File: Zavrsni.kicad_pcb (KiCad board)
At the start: 2 copper layers, 70 x 133.3 mm, 42 parts, among them K1 JST-2pin-SMD, SW1 SW_Push, SW2 SW_Push, SW3 Power_switch

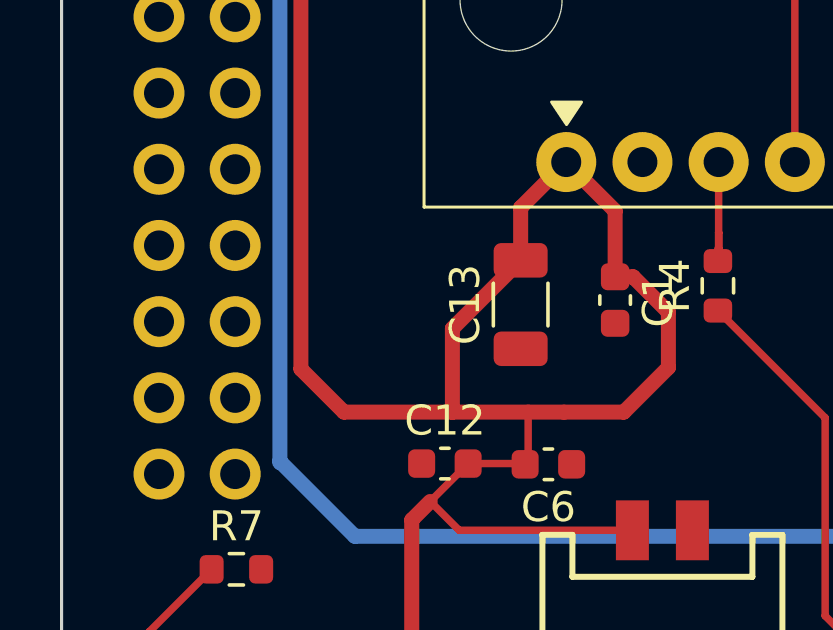
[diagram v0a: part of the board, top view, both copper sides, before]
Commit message: switch error, the wrong switch was selected and connected incorrectly in the schematic
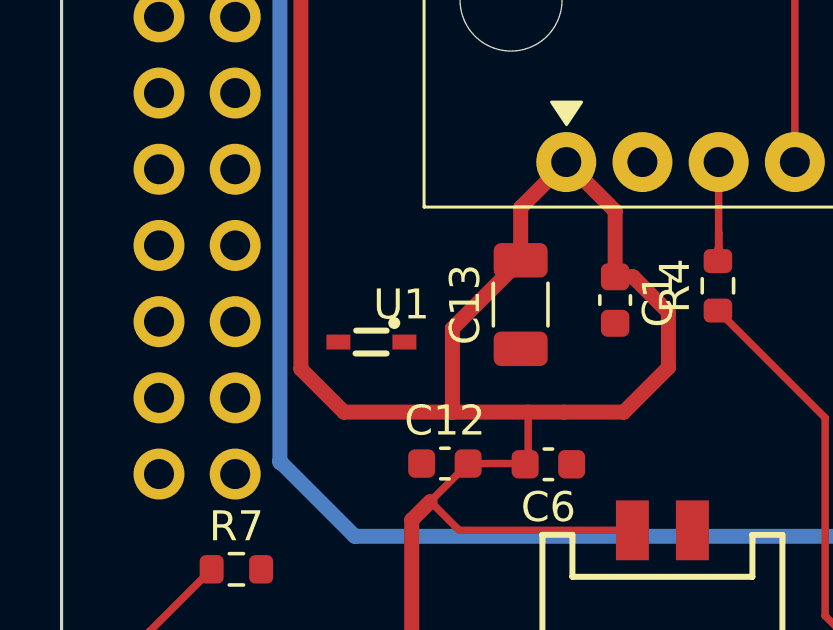
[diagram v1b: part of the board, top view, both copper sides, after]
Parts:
- added U1: Shottky_Diode, Schottky_Diode:Sh_D bat20, F.Cu at (75.2, 145.2)
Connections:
- NUCLEO_144_H743ZI2 pad 15: unconnected-(NUCLEO_144_H743ZI2-VIN-Pad15) -> /VIN

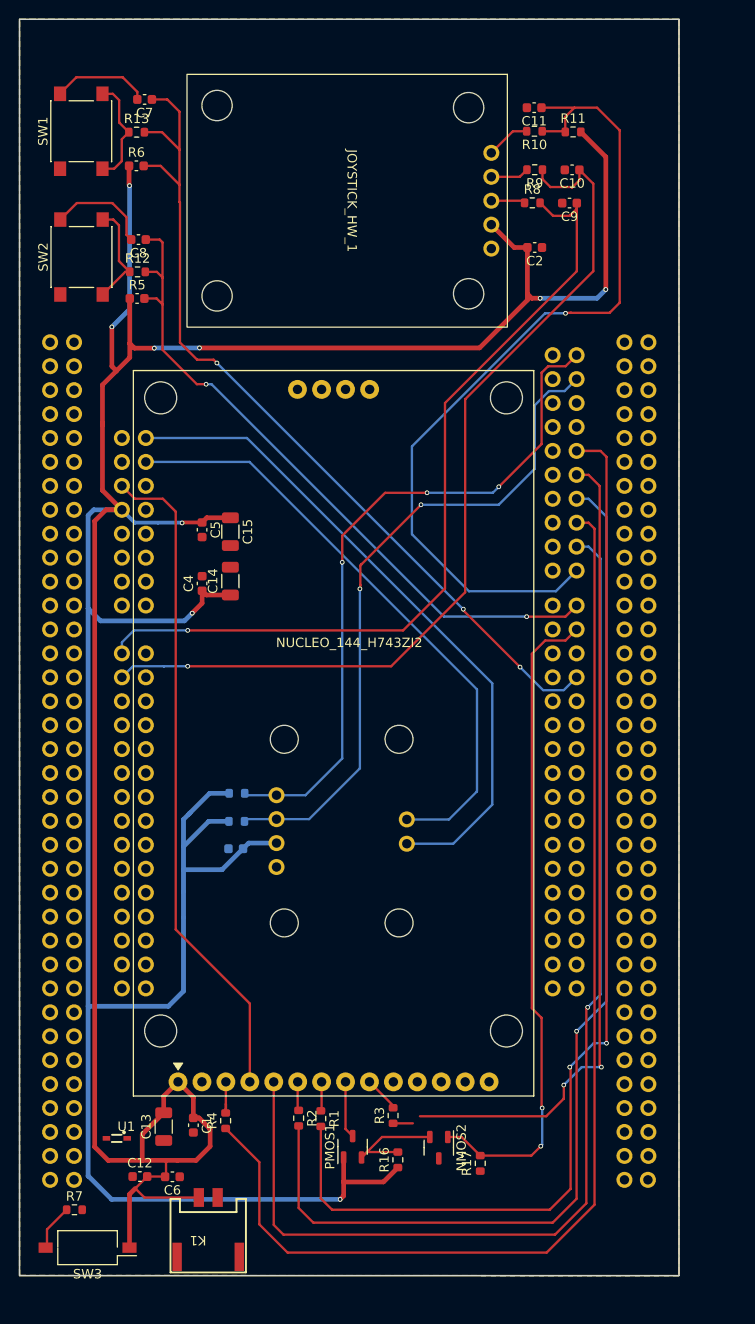
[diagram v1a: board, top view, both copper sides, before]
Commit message: Shifted pins on the nucleo board, up the y axis
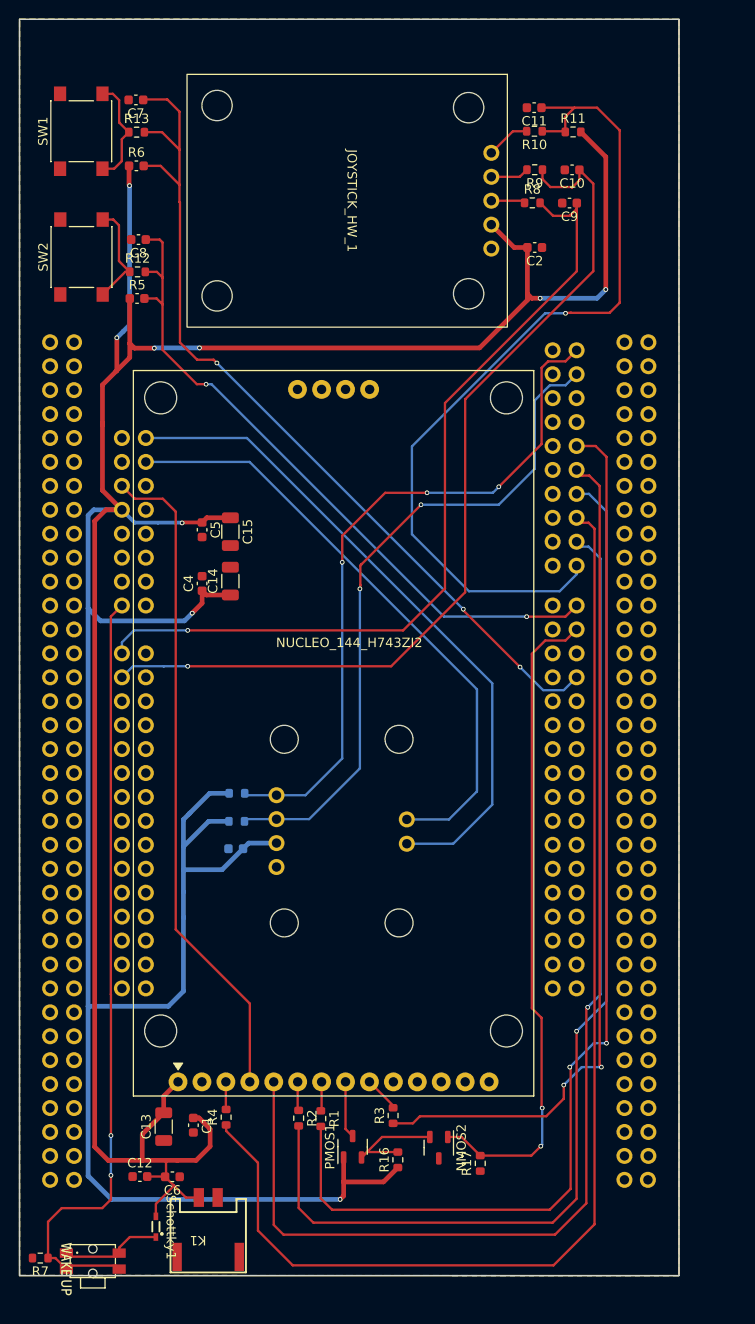
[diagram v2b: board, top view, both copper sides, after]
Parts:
- removed SW3: Power_switch, Button_Switch_SMD:SW_DIP_SPSTx01_Slide_Omron_A6S-110x_W8.9mm_P2.54mm
- removed U1: Shottky_Diode, Schottky_Diode:Sh_D bat20
- added Schottky1: ~, Schottky_D:Schottky_D, F.Cu at (79.5, 154.5)
- added Wake_up1: ~, Power_Switch:Power_Switch, F.Cu at (72.8, 158.8)
- moved R7 6.28 mm to (67.1, 157.8), turned to 180 degrees
- moved C7 0.93 mm to (77.3, 34.9)
- moved R4 0.38 mm to (86.8, 142.9)
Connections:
- NUCLEO_144_H743ZI2 pad 27: (no net) -> unconnected-(NUCLEO_144_H743ZI2-A5-Pad27)
- NUCLEO_144_H743ZI2 pad 30: (no net) -> unconnected-(NUCLEO_144_H743ZI2-PE2-Pad30)
- NUCLEO_144_H743ZI2 pad 94: (no net) -> unconnected-(NUCLEO_144_H743ZI2-PE_12(SCK/SPI4)-Pad94)
- R7 pad 1: Net-(R7-Pad1) -> /VIN
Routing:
- net /VIN: track 0.00 -> 83.4 mm, vias 0 -> 2
- net Earth: track 21.5 -> 0.22 mm
- net +3.3V: track 445.7 -> 433.9 mm
- net Net-(Schottky1-C): track 0.00 -> 10.8 mm
- net Net-(R7-Pad1): track 4.89 -> 0.00 mm
- net /CSN: track 124.5 -> 127.9 mm
- net /SDO(MISO): track 89.1 -> 90.4 mm
- net /D4: track 95.2 -> 96.2 mm
- net /CS: track 3.87 -> 2.94 mm
- net /SW: track 91.8 -> 92.5 mm
- net /SDI(MOSI): track 117.6 -> 118.1 mm
- net /D15: track 72.9 -> 73.5 mm
- net /D14: track 71.3 -> 71.8 mm

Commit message: The pcb is assembled, but the pin spacing is incorrect
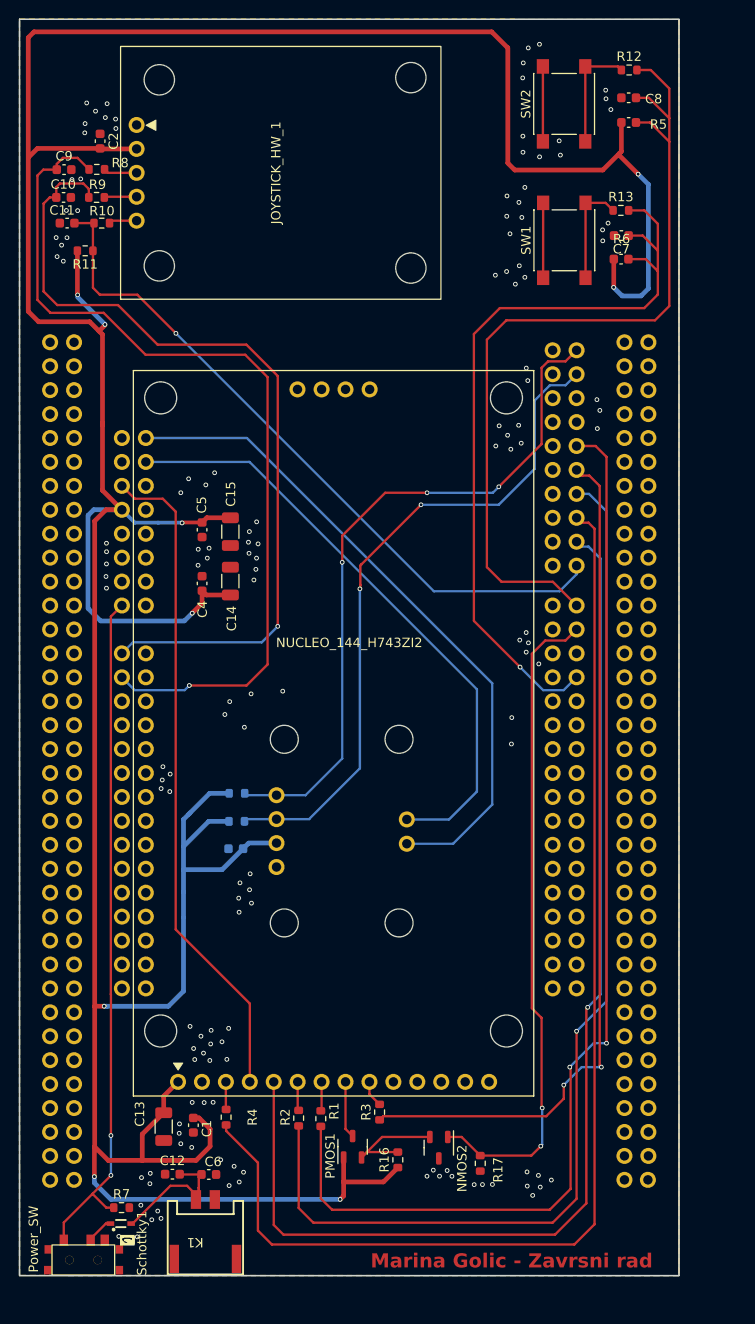
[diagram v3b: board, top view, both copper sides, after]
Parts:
- removed Wake_up1: ~, Power_Switch:Power_Switch
- added SW_Power1: ~, Power_Switch:Power_Switch, F.Cu at (72.0, 157.7)
- moved R12 56.4 mm to (129.6, 31.8)
- moved R5 55.4 mm to (129.6, 37.3)
- moved C8 54.2 mm to (129.6, 34.7)
- moved C10 54.1 mm to (69.6, 45.3), turned to 0 degrees
- moved C9 53.8 mm to (69.7, 42.3), turned to 0 degrees
- moved SW2 53.7 mm to (122.7, 35.4)
- moved C7 53.5 mm to (128.8, 49.3)
- moved R11 53.3 mm to (71.9, 50.9), turned to 180 degrees
- moved SW1 52.6 mm to (122.8, 49.8)
- moved R6 52.4 mm to (128.8, 51.8)
- moved R13 52.1 mm to (128.8, 46.6)
- moved C11 51.1 mm to (70.0, 48.0)
- moved C2 47.5 mm to (73.5, 39.3), turned to -90 degrees
- moved R10 46.9 mm to (73.7, 48.0), turned to 0 degrees
- moved R9 46.6 mm to (73.1, 45.3), turned to 0 degrees
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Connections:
- net /INT1 renamed /PC_8
- net /INT2 renamed /PC_9
- C12 pad 2: +3.3V -> /VBAT
- C6 pad 2: +3.3V -> /VBAT
- K1 pad 1: +3.3V -> /VBAT
- NUCLEO_144_H743ZI2 pad 17: /VRx -> /VRy
- NUCLEO_144_H743ZI2 pad 19: /VRy -> /VRx
- NUCLEO_144_H743ZI2 pad 28: unconnected-(NUCLEO_144_H743ZI2-GND-Pad28) -> Earth
- NUCLEO_144_H743ZI2 pad 71: unconnected-(NUCLEO_144_H743ZI2-GND-Pad71) -> Earth
- Schottky1 pad 1: +3.3V -> /VBAT
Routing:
- net /D7: track 73.8 -> 92.3 mm, vias 2 -> 0
- net /SW: track 92.5 -> 75.3 mm
- net +3.3V: track 433.9 -> 417.4 mm
- net /VBAT: track 0.00 -> 15.7 mm
- net Earth: track 0.22 -> 15.9 mm, vias 0 -> 144
- net /D4: track 96.2 -> 84.9 mm, vias 3 -> 1
- net /VIN: track 83.4 -> 72.8 mm
- net /VRy: track 98.0 -> 89.7 mm
- net Net-(Schottky1-C): track 10.8 -> 2.92 mm
- net /VRx: track 89.9 -> 95.8 mm
- net /CSN: track 127.9 -> 126.0 mm
- net /T1: track 4.70 -> 2.98 mm
- net /SDO(MISO): track 90.4 -> 91.7 mm
- net /SDO: track 3.79 -> 2.83 mm
- net Net-(R12-Pad1): track 11.3 -> 11.9 mm
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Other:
- board text added: "Marina Golic - Zavrsni rad"

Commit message: The pcb is cut for the buttons on the NUCLEO board
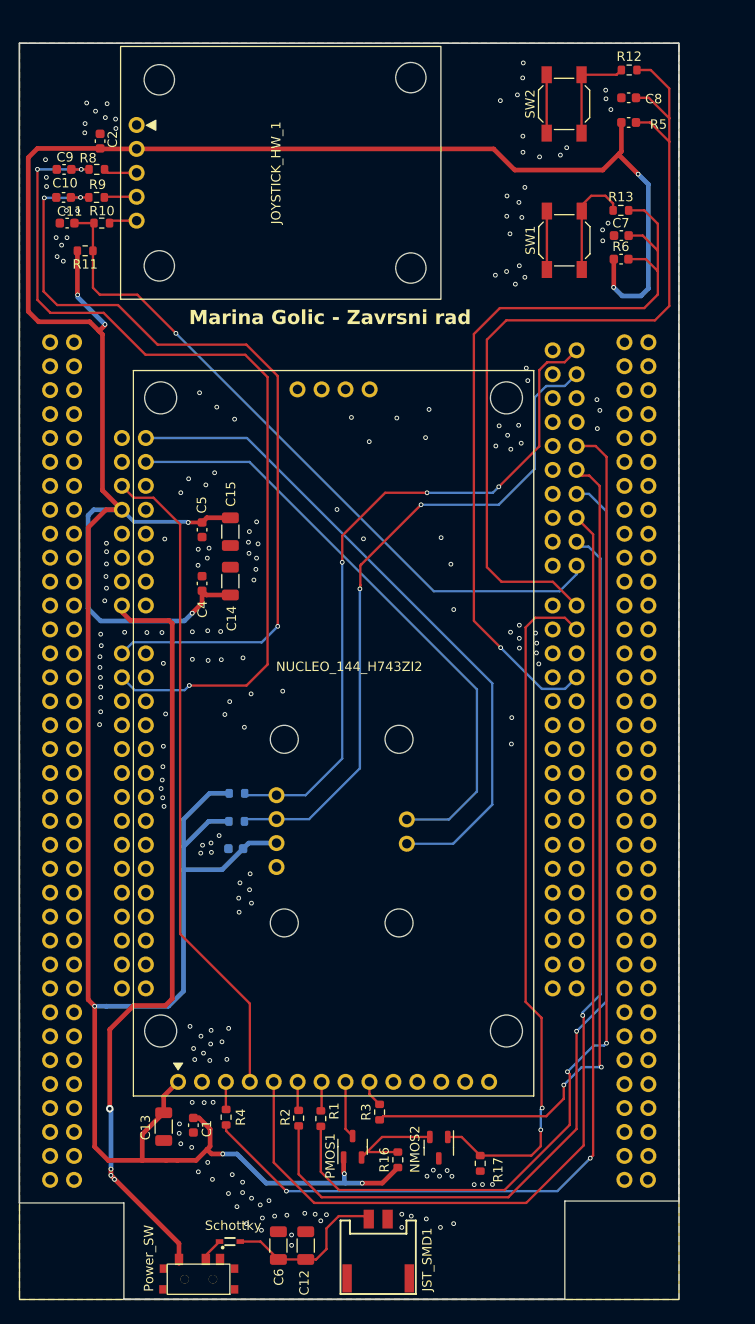
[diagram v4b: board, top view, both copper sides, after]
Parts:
- removed K1: JST-2pin-SMD, JST conector:jst connector
- removed R7: 220K, Resistor_SMD:R_0603_1608Metric
- added JST_SMD1: ~, JST_connector_SMD:JST_SMD, F.Cu at (102.7, 157.9)
- C12, C6: footprint Capacitor_SMD:C_0603_1608Metric -> Capacitor_SMD:C_1206_3216Metric
- SW1, SW2: footprint Button_Switch_SMD:SW_Push_1P1T_NO_6x6mm_H9.5mm -> Button_Switch_SMD:SW_SPST_SKQG_WithoutStem
- moved C12 16.1 mm to (95.3, 156.5), turned to -90 degrees
- moved SW_Power1 12.4 mm to (84.2, 159.7)
- moved Schottky 11.7 mm to (87.3, 156.2)
- moved C6 10.6 mm to (92.4, 156.5), turned to -90 degrees
- moved NUCLEO_144_H743ZI2 2.54 mm to (99.9, 95.6)
- turned C9 to 180 degrees
- turned C10 to 180 degrees
- renumbered Schottky1 to Schottky
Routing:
- net +3.3V: track 417.4 -> 364.4 mm, vias 9 -> 10
- net /CSN: track 126.0 -> 112.2 mm, vias 0 -> 2
- net /DC/RS: track 122.6 -> 112.2 mm
- net /VIN: track 72.8 -> 82.7 mm, vias 2 -> 4
- net /SDI(MOSI): track 118.1 -> 109.5 mm
- net /SCK(D13): track 119.5 -> 111.9 mm
- net /LED(PWM): track 69.7 -> 73.3 mm
- net Earth: track 15.9 -> 12.4 mm, vias 144 -> 198
- net /VBAT: track 15.7 -> 17.8 mm
- net Net-(R12-Pad1): track 11.9 -> 10.6 mm
- net /VRy: track 89.7 -> 88.7 mm, vias 1 -> 3
- net /NRST: track 70.6 -> 70.1 mm
- net /VRx: track 95.8 -> 95.9 mm, vias 1 -> 3
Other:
- outline, holes or cut-outs redrawn

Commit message: Finnal version of PCB and schema
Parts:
- renumbered Schottky to Schottky1
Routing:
- net +3.3V: track 364.4 -> 380.7 mm, vias 10 -> 11
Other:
- board text added: "+"
- board text added: "-"
- board text added: "VBAT"
- board text added: "VIN"

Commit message: Finall version of PCB without gerbers
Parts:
- renumbered Schottky1 to D1
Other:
- board text added: "Marina Golic - Zavrsni - 20.8.2023"
- board text added: "Marina Golic - Zavrsni rad - 20.8.2023"
- board text removed: "Marina Golic - Zavrsni rad"
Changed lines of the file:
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@@
     (property "ki_keywords" "R res resistor")
     (attr smd)
-    (fp_text reference "R5" (at 0 -1.43) (layer "F.SilkS")
+    (fp_text reference "R5" (at -0.04 -1.252) (layer "F.SilkS")
         (effects (font (size 1 1) (thickness 0.15)))
     )
@@
     (property "ki_keywords" "R res resistor")
     (attr smd)
-    (fp_text reference "R4" (at 0 -1.43 90) (layer "F.SilkS")
+    (fp_text reference "R4" (at -0.102 -1.252 90) (layer "F.SilkS")
         (effects (font (size 1 1) (thickness 0.15)))
     )
@@
     (property "ki_keywords" "cap capacitor")
     (attr smd)
-    (fp_text reference "C8" (at 0 -1.43 180) (layer "F.SilkS")
+    (fp_text reference "C8" (at 0 1.426 180) (layer "F.SilkS")
         (effects (font (size 1 1) (thickness 0.15)))
     )
@@
     (property "ki_keywords" "R res resistor")
     (attr smd)
-    (fp_text reference "R6" (at 0 -1.43) (layer "F.SilkS")
+    (fp_text reference "R6" (at 0.003 -1.279) (layer "F.SilkS")
         (effects (font (size 1 1) (thickness 0.15)))
     )
@@
         (effects (font (size 1 1) (thickness 0.15)))
     )
-    (fp_text user "SW_power" (at 5.958 1.204 90 unlocked) (layer "F.SilkS")
+    (fp_text user "SW_power" (at 5.958 1.458 90 unlocked) (layer "F.SilkS")
         (effects (font (size 1 1) (thickness 0.15)))
     )
@@
     (property "ki_keywords" "cap capacitor")
     (attr smd)
-    (fp_text reference "C6" (at 0 -1.85 -90) (layer "F.SilkS")
+    (fp_text reference "C6" (at 3.241 -0.056 -90) (layer "F.SilkS")
         (effects (font (size 1 1) (thickness 0.15)))
     )
@@
     (property "ki_keywords" "R res resistor")
     (attr smd)
-    (fp_text reference "R1" (at 0 -1.43 -90) (layer "F.SilkS")
+    (fp_text reference "R1" (at 0 1.142 -90) (layer "F.SilkS")
         (effects (font (size 1 1) (thickness 0.15)))
     )
@@
     (property "Sheetname" "")
     (attr smd)
-    (fp_text reference "PMOS1" (at 0 -2.4 90) (layer "F.SilkS")
+    (fp_text reference "PMOS1" (at -0.5205 -2.231 90) (layer "F.SilkS")
         (effects (font (size 1 1) (thickness 0.15)))
     )
@@
     (property "ki_keywords" "cap capacitor")
     (attr smd)
-    (fp_text reference "C7" (at 0 -1.43 180) (layer "F.SilkS")
+    (fp_text reference "C7" (at 0 1.319 180) (layer "F.SilkS")
         (effects (font (size 1 1) (thickness 0.15)))
     )
@@
     (property "ki_keywords" "cap capacitor")
     (attr smd)
-    (fp_text reference "C1" (at 0 -1.43 -90) (layer "F.SilkS")
+    (fp_text reference "C1" (at -1.51 1.333 -90) (layer "F.SilkS")
         (effects (font (size 1 1) (thickness 0.15)))
     )
@@
     (property "ki_keywords" "cap capacitor")
     (attr smd)
-    (fp_text reference "C5" (at 0 -1.43 -90) (layer "F.SilkS")
+    (fp_text reference "C5" (at -2.318 -0.028 -90) (layer "F.SilkS")
         (effects (font (size 1 1) (thickness 0.15)))
     )
@@
     (property "ki_keywords" "R res resistor")
     (attr smd)
-    (fp_text reference "R2" (at 0 -1.43 -90) (layer "F.SilkS")
+    (fp_text reference "R2" (at 0 1.332 -90) (layer "F.SilkS")
         (effects (font (size 1 1) (thickness 0.15)))
     )
@@
     (property "Sheetname" "")
     (attr smd)
-    (fp_text reference "NMOS2" (at 0 -2.4 -90) (layer "F.SilkS")
+    (fp_text reference "NMOS2" (at 0.4205 2.237 -90) (layer "F.SilkS")
         (effects (font (size 1 1) (thickness 0.15)))
     )
@@
     (property "ki_keywords" "cap capacitor")
     (attr smd)
-    (fp_text reference "C14" (at 0 -1.85 90) (layer "F.SilkS")
+    (fp_text reference "C14" (at -0.36 1.854 90) (layer "F.SilkS")
         (effects (font (size 1 1) (thickness 0.15)))
     )
@@
     (property "Sheetname" "")
     (attr smd)
-    (fp_text reference "Schottky1" (at 0.1 -1.5 180 unlocked) (layer "F.SilkS")
-        (effects (font (size 1 1) (thickness 0.1)))
+    (fp_text reference "D1" (at -0.076 1.26 unlocked) (layer "F.SilkS")
+        (effects (font (size 1 1) (thickness 0.2) bold))
     )
     (fp_text value "~" (at 0 1 180 unlocked) (layer "F.Fab")
-        (effects (font (size 1 1) (thickness 0.15)))
+        (effects (font (size 1 1) (thickness 0.2) bold))
     )
     (fp_text user "${REFERENCE}" (at 0.25 2.8 180 unlocked) (layer "F.Fab")
@@
     (property "ki_keywords" "cap capacitor")
     (attr smd)
-    (fp_text reference "C3" (at 0 1.43 180) (layer "B.SilkS")
+    (fp_text reference "C3" (at 0.009 -1.37 180) (layer "B.SilkS")
         (effects (font (size 1 1) (thickness 0.15)) (justify mirror))
     )
@@
     (property "ki_keywords" "R res resistor")
     (attr smd)
-    (fp_text reference "R14" (at 0 1.43 180) (layer "B.SilkS")
+    (fp_text reference "R14" (at 0 -1.591 180) (layer "B.SilkS")
         (effects (font (size 1 1) (thickness 0.15)) (justify mirror))
     )
@@
   (gr_rect (start 148.175 96.225) (end 148.175 96.225)
     (stroke (width 0.1) (type default)) (fill none) (layer "Edge.Cuts"))
-  (gr_text "Marina Golic - Zavrsni rad\n" (at 114.6 59.4) (layer "B.SilkS")
+  (gr_text "Marina Golic - Zavrsni  - 20.8.2023\n\n" (at 122.428 61.468) (layer "B.SilkS")
     (effects (font (size 1.5 1.5) (thickness 0.3) bold) (justify left bottom mirror))
-  )
-  (gr_text "-" (at 107.188 153.416) (layer "B.SilkS")
-    (effects (font (size 1 1) (thickness 0.15)) (justify left bottom mirror))
   )
   (gr_text "+" (at 101.092 153.416) (layer "F.SilkS")
@@
     (effects (font (size 1 1) (thickness 0.125)) (justify left bottom))
   )
-  (gr_text "Marina Golic - Zavrsni rad\n" (at 87.884 61.468) (layer "F.SilkS")
+  (gr_text "Marina Golic - Zavrsni rad - 20.8.2023\n" (at 76.454 59.436) (layer "F.SilkS")
     (effects (font (size 1.5 1.5) (thickness 0.3) bold) (justify left bottom))
   )
@@
     (effects (font (size 1 1) (thickness 0.1875)) (justify left bottom))
   )
+  (gr_text "-" (at 107.188 153.416) (layer "F.SilkS")
+    (effects (font (size 1 1) (thickness 0.15)) (justify left bottom mirror))
+  )
   (segment (start 128 54.8) (end 127.98 54.82) (width 0.25) (layer "F.Cu") (net 1))
